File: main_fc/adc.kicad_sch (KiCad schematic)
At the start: 23 parts, among them J2 Conn_01x16_Pin, J3 Conn_01x08_Pin, J5 Conn_01x08_Pin, U1 ADS1158IRTCR (ADC), Y1 32.768kHz

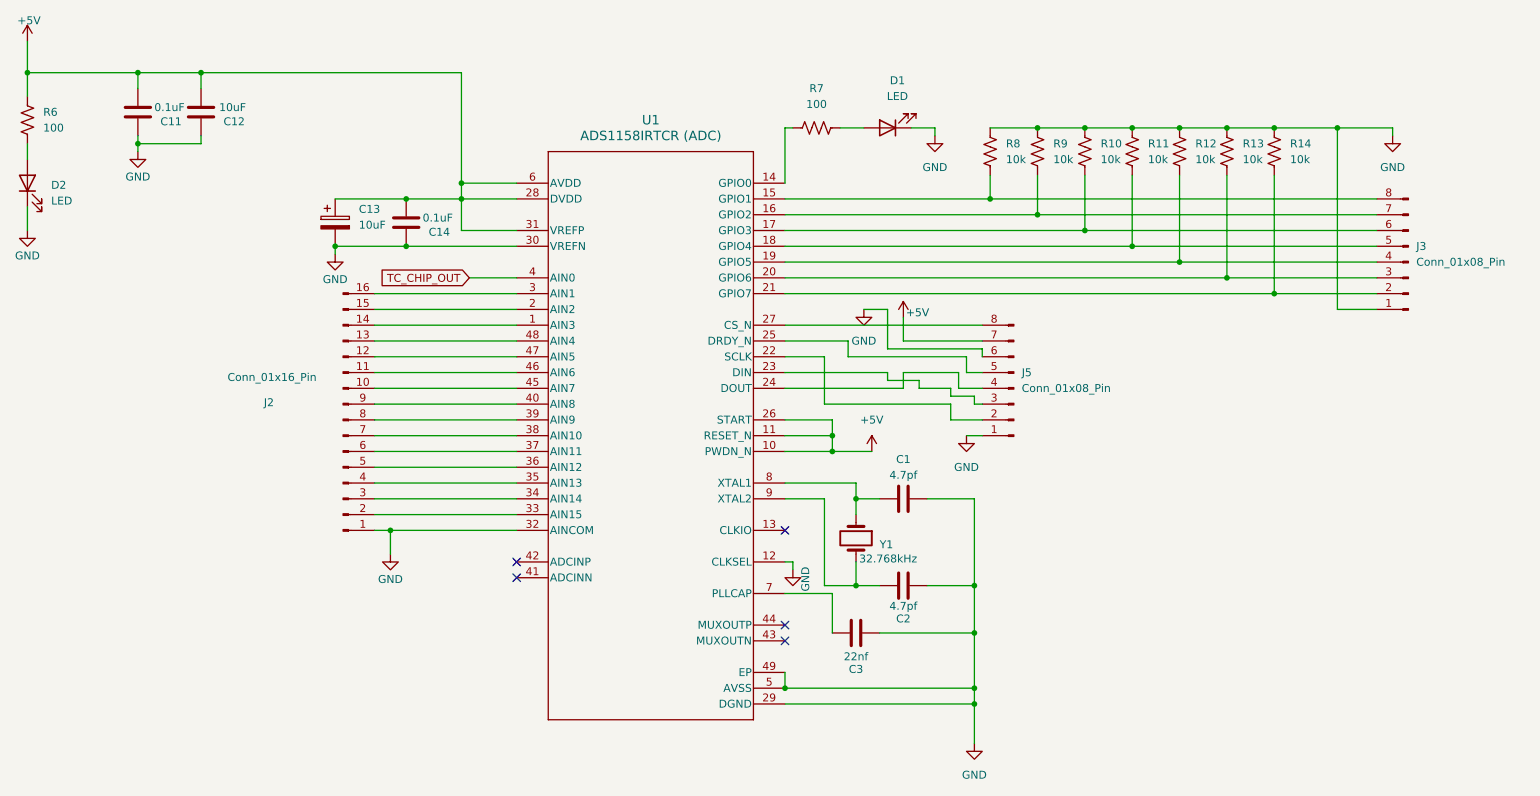
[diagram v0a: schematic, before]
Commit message: main flight computer annotations and passive footprints
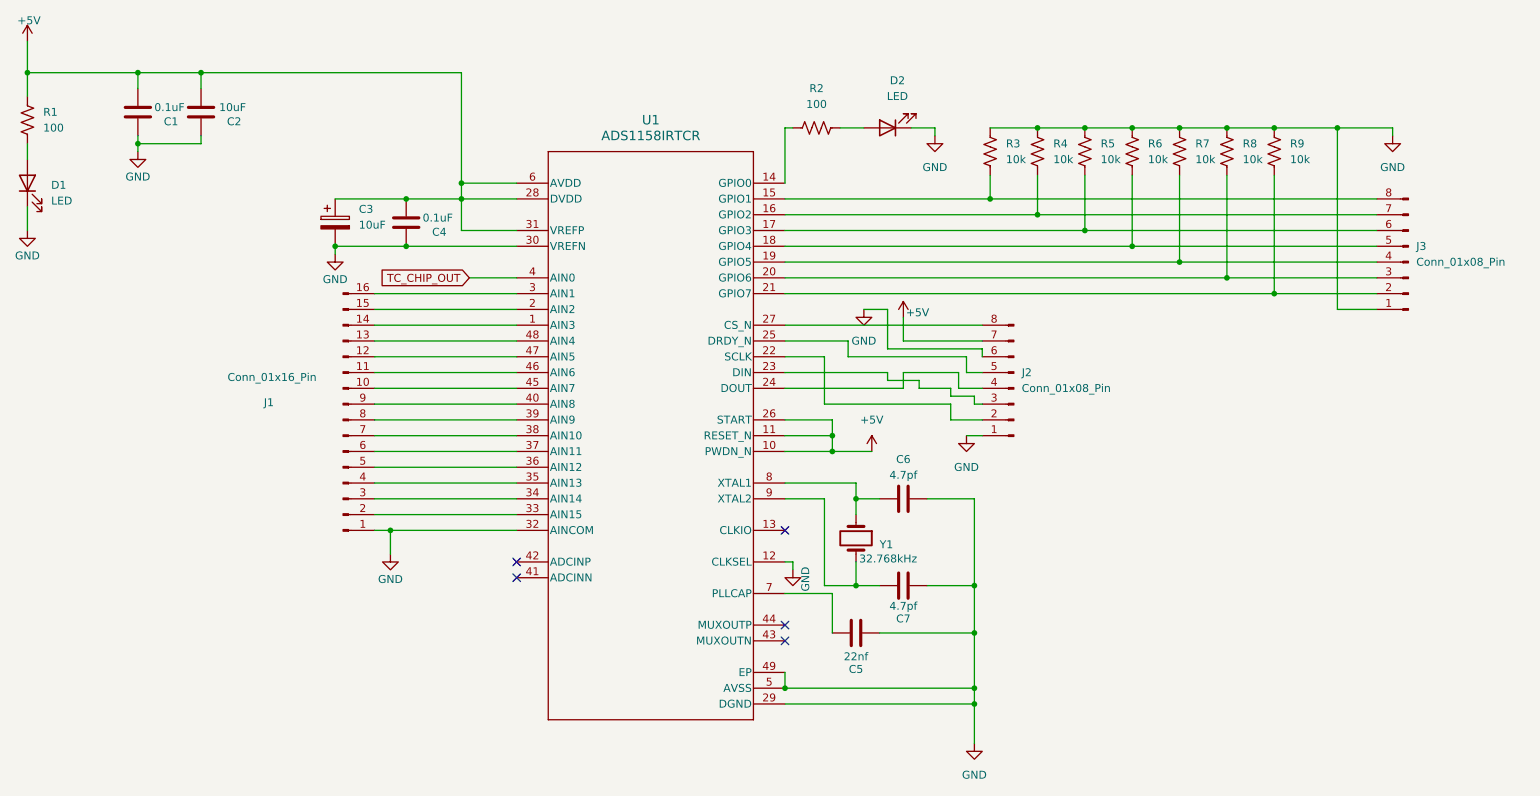
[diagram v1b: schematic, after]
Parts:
- R1: renamed from R6; footprint Resistor_SMD:R_0201_0603Metric -> Resistor_SMD:R_0603_1608Metric
- R2: renamed from R7; footprint Resistor_SMD:R_0201_0603Metric -> Resistor_SMD:R_0603_1608Metric
- R3: renamed from R8; footprint Resistor_SMD:R_0201_0603Metric -> Resistor_SMD:R_0603_1608Metric
- R4: renamed from R9; footprint Resistor_SMD:R_0201_0603Metric -> Resistor_SMD:R_0603_1608Metric
- R5: renamed from R10; footprint Resistor_SMD:R_0201_0603Metric -> Resistor_SMD:R_0603_1608Metric
- R6: renamed from R11; footprint Resistor_SMD:R_0201_0603Metric -> Resistor_SMD:R_0603_1608Metric
- R7: renamed from R12; footprint Resistor_SMD:R_0201_0603Metric -> Resistor_SMD:R_0603_1608Metric
- R8: renamed from R13; footprint Resistor_SMD:R_0201_0603Metric -> Resistor_SMD:R_0603_1608Metric
- R9: renamed from R14; footprint Resistor_SMD:R_0201_0603Metric -> Resistor_SMD:R_0603_1608Metric
- U1: value ADS1158IRTCR (ADC) -> ADS1158IRTCR
- renumbered C11 to C1, C12 to C2, C13 to C3, C14 to C4, C3 to C5, C1 to C6, C2 to C7, D2 to D1, D1 to D2, J2 to J1, J5 to J2

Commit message: updated library
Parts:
- removed J1: Conn_01x16_Pin, Connector_PinHeader_2.54mm:PinHeader_1x16_P2.54mm_Vertical, symbol Connector:Conn_01x16_Pin
- removed J2, J3: Conn_01x08_Pin, Connector_PinHeader_2.54mm:PinHeader_1x08_P2.54mm_Vertical, symbol Connector:Conn_01x08_Pin
- U1: footprint ul_ADS1158IRTCR:RTC0048A-IPC_A -> avi_footprint:RTC0048A-IPC_C

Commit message: updated TC routing
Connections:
- net AIN3: now reaches U1.1 (AIN3)
- net AIN2: now reaches U1.2 (AIN2)
- net AIN1: now reaches U1.3 (AIN1)
- net AIN15: now reaches U1.33 (AIN15)
- net AIN14: now reaches U1.34 (AIN14)
- net AIN13: now reaches U1.35 (AIN13)
- net AIN12: now reaches U1.36 (AIN12)
- net AIN11: now reaches U1.37 (AIN11)
- net AIN10: now reaches U1.38 (AIN10)
- net AIN9: now reaches U1.39 (AIN9)
- net AIN8: now reaches U1.40 (AIN8)
- net AIN7: now reaches U1.45 (AIN7)
- net AIN6: now reaches U1.46 (AIN6)
- net AIN5: now reaches U1.47 (AIN5)
- net AIN4: now reaches U1.48 (AIN4)
- net TC_CHIP_OUT renamed AIN0
